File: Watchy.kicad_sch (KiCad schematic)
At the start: 67 parts, among them J1 FPC24(0.5MM), J2 Micro USB, J3 Battery, M1 Vibration_Motor, Q1 AO3400A, Q2 UMH3N, Q4 CJ2301, Q5 S8050, SW1 BTN, SW2 BTN, SW3 BTN, SW4 BTN, U1 ESP32-PICO-D4, U2 ME6211C33M5G-N, U3 CP2102, U4 BMA423, U5 TP4054, U6 PCF8563BS, Y1 32.768KHz

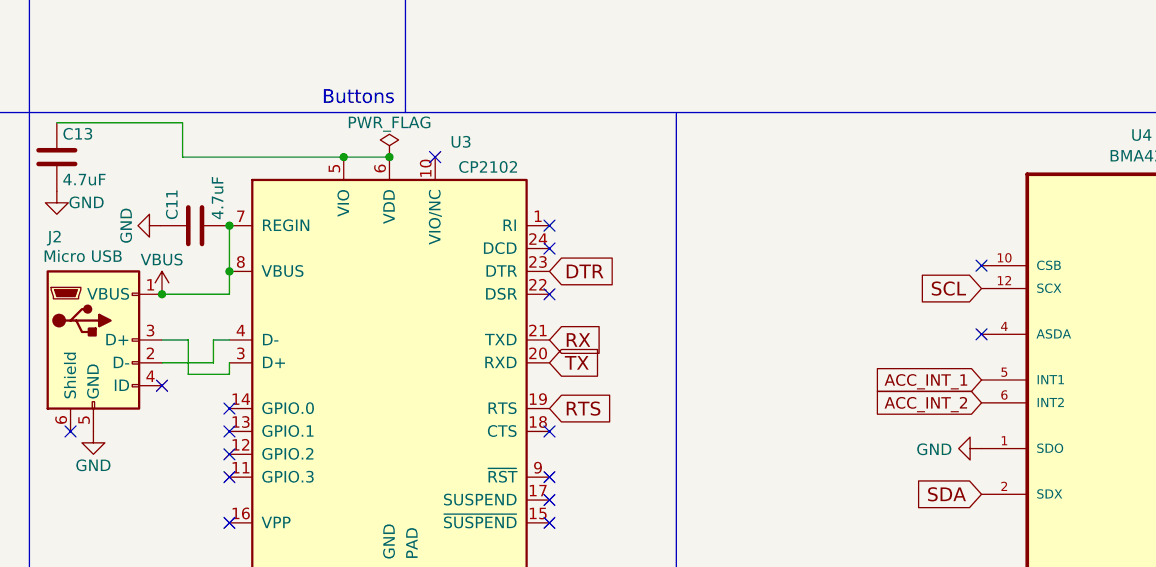
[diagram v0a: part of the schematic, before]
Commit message: cleanup of USB data lines
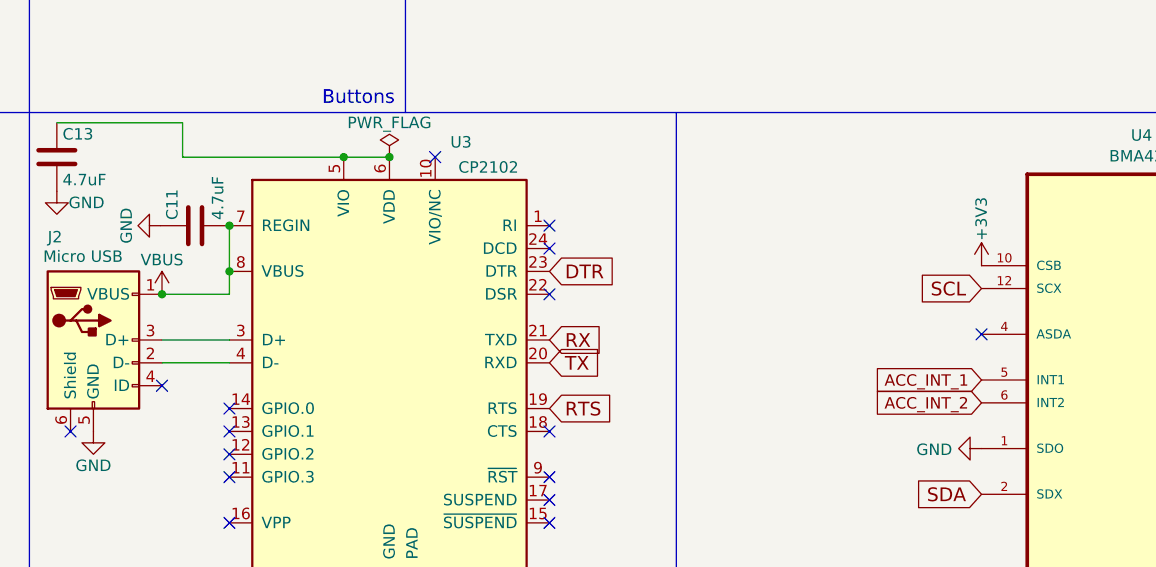
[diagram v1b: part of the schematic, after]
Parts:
- U3: footprint Housings_DFN_QFN:QFN-24-1EP_4x4mm_Pitch0.5mm -> Package_DFN_QFN:QFN-24-1EP_4x4mm_P0.5mm_EP2.6x2.6mm
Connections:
- net +3V3: now also U4.10 (CSB)
- no-connect marks 37 -> 36
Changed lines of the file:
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@@
   (no_connect (at 34.29 75.946))
   (no_connect (at 74.93 96.266))
-  (no_connect (at 210.947 127.889))
   (no_connect (at 34.29 70.866))
   (no_connect (at 162.941 146.304))
@@
     (stroke (width 0) (type default))
   )
-  (wire (pts (xy 119.888 136.144) (xy 122.809 136.144))
+  (wire (pts (xy 119.888 136.144) (xy 127.381 136.144))
     (stroke (width 0) (type default))
   )
@@
     (stroke (width 0) (type default))
   )
-  (wire (pts (xy 122.809 139.954) (xy 127.381 139.954))
-    (stroke (width 0) (type default))
-  )
-  (wire (pts (xy 125.603 136.144) (xy 127.381 136.144))
-    (stroke (width 0) (type default))
-  )
-  (wire (pts (xy 127.381 139.954) (xy 127.381 138.684))
-    (stroke (width 0) (type default))
-  )
-  (wire (pts (xy 122.809 136.144) (xy 122.809 139.954))
-    (stroke (width 0) (type default))
-  )
   (wire (pts (xy 19.304 185.42) (xy 19.304 187.96))
     (stroke (width 0) (type default))
@@
     (stroke (width 0) (type default))
   )
-  (wire (pts (xy 119.888 138.684) (xy 125.603 138.684))
+  (wire (pts (xy 119.888 138.684) (xy 127.381 138.684))
     (stroke (width 0) (type default))
   )
@@
     (stroke (width 0) (type default))
   )
-  (wire (pts (xy 125.603 138.684) (xy 125.603 136.144))
-    (stroke (width 0) (type default))
-  )
   (polyline (pts (xy 105.156 12.319) (xy 105.156 169.037))
     (stroke (width 0) (type default))
@@
       (effects (font (size 1.27 1.27)) (justify right))
     )
-    (property "Footprint" "Housings_DFN_QFN:QFN-24-1EP_4x4mm_Pitch0.5mm" (at 148.971 162.814 0)
+    (property "Footprint" "Package_DFN_QFN:QFN-24-1EP_4x4mm_P0.5mm_EP2.6x2.6mm" (at 148.971 162.814 0)
       (effects (font (size 1.27 1.27)) (justify left) hide)
     )
@@
         )
       )
+    )
+  )
+  (symbol (lib_id "power:+3V3") (at 210.947 127.889 0) (unit 1)
+    (in_bom yes) (on_board yes) (dnp no)
+    (property "Reference" "#PWR067" (at 210.947 131.699 0)
+      (effects (font (size 1.27 1.27)) hide)
+    )
+    (property "Value" "+3V3" (at 210.947 122.682 90)
+      (effects (font (size 1.27 1.27)))
+    )
+    (property "Footprint" "" (at 210.947 127.889 0)
+      (effects (font (size 1.27 1.27)) hide)
+    )
+    (property "Datasheet" "" (at 210.947 127.889 0)
+      (effects (font (size 1.27 1.27)) hide)
+    )
+    (pin "1")
+    (instances
+      (project "Watchy"
+        (path "/4168ccf9-7940-46a9-babd-bad8c703bb50"
+          (reference "#PWR067") (unit 1)
+        )
+      )

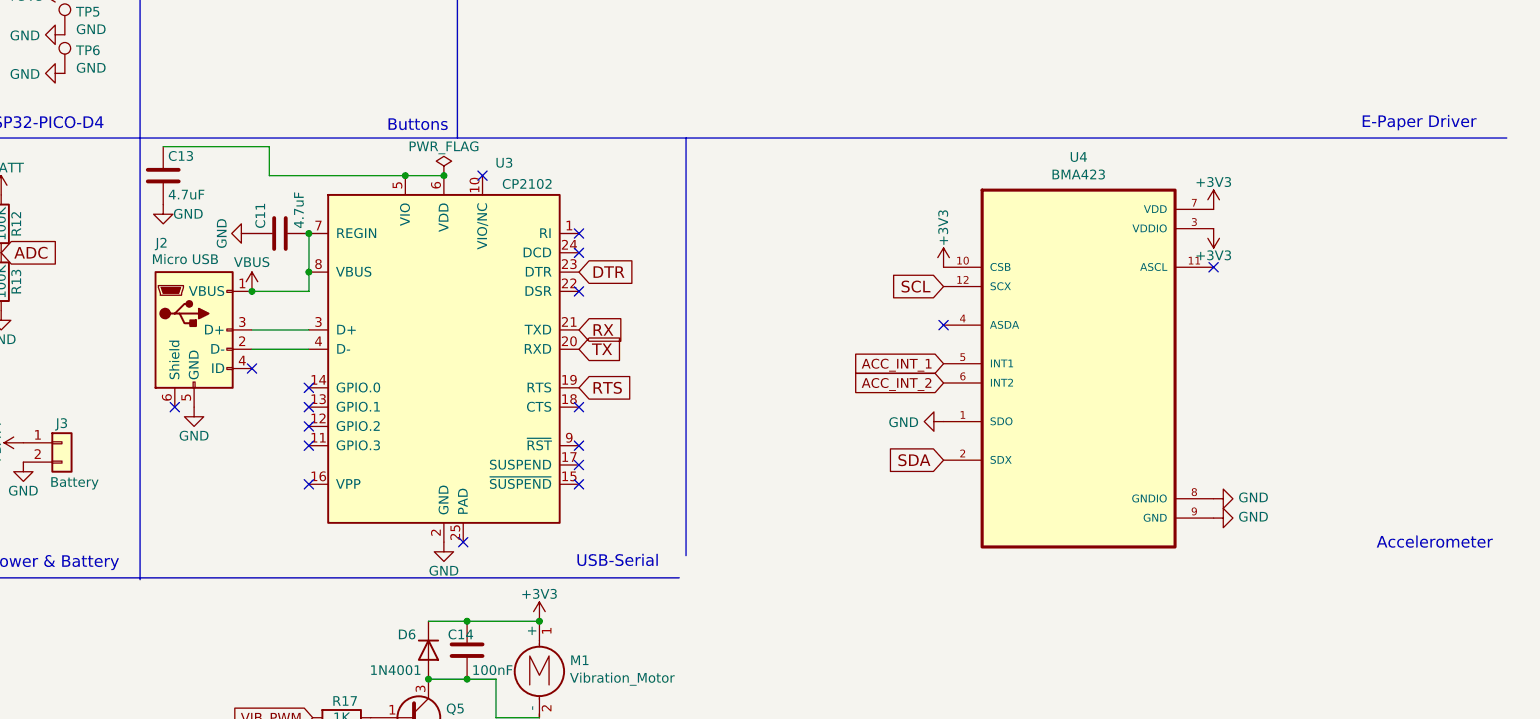
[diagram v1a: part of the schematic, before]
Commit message: replace micro usb with usb c in schematic
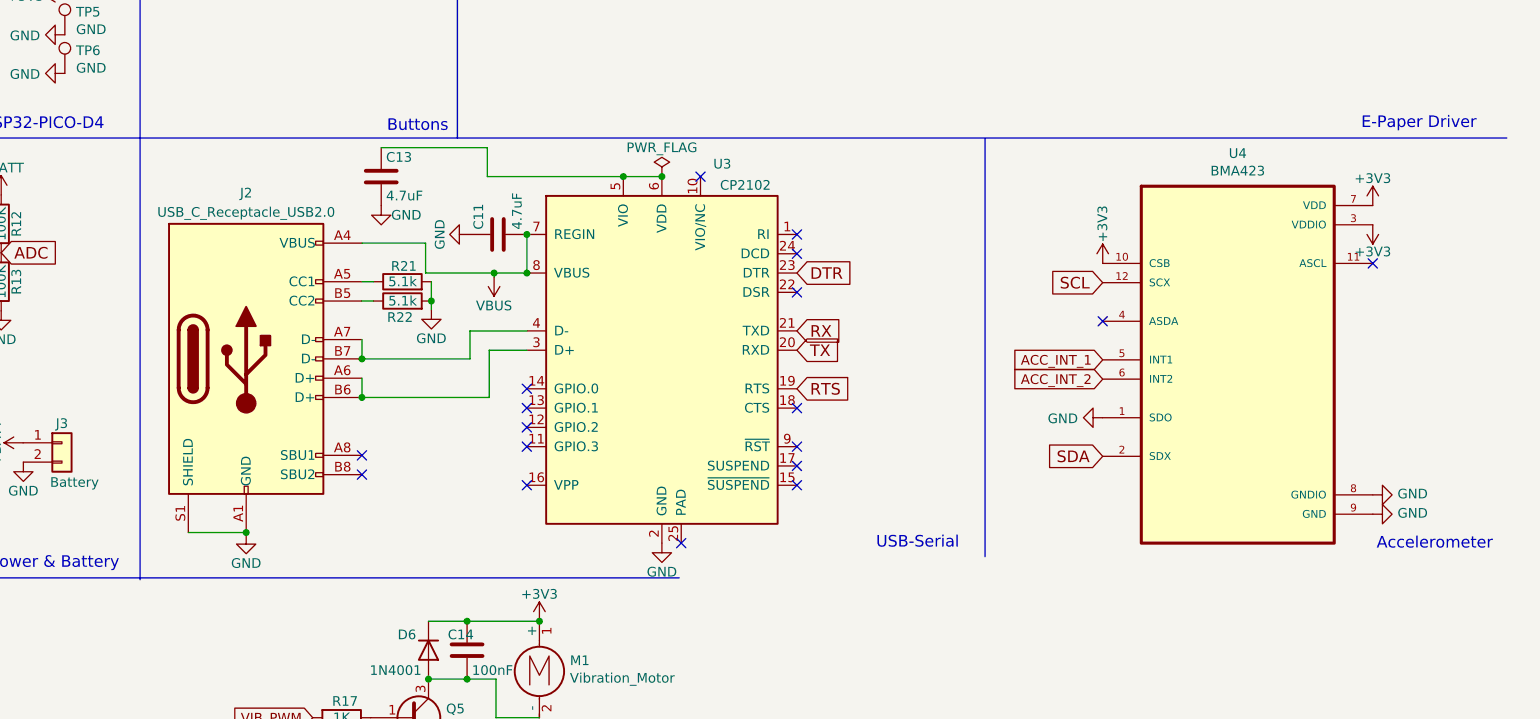
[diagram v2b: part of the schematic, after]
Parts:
- removed J2: Micro USB, Watchy:USB_Micro-B, symbol Connector:USB_OTG
- added J2: USB_C_Receptacle_USB2.0, Connector_USB:USB_C_Receptacle_Palconn_UTC16-G, symbol Connector:USB_C_Receptacle_USB2.0
- added R21, R22: 5.1k, Resistors_SMD:R_0402, symbol Device:R
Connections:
- net GND: now also J2.A1 (GND), J2.A12 (GND), J2.B1 (GND), J2.B12 (GND), J2.S1 (SHIELD), R21.2, R22.2
- net VBUS: now also J2.A4 (VBUS), J2.A9 (VBUS), J2.B4 (VBUS), J2.B9 (VBUS)
- net at U3.4 (D-): now also J2.A7 (D-), J2.B7 (D-)
- net at U3.3 (D+): now also J2.A6 (D+), J2.B6 (D+)
- new net: J2.B5 (CC2), R22.1
- new net: J2.A5 (CC1), R21.1
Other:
- moved on the sheet: C11, C13, U3, U4

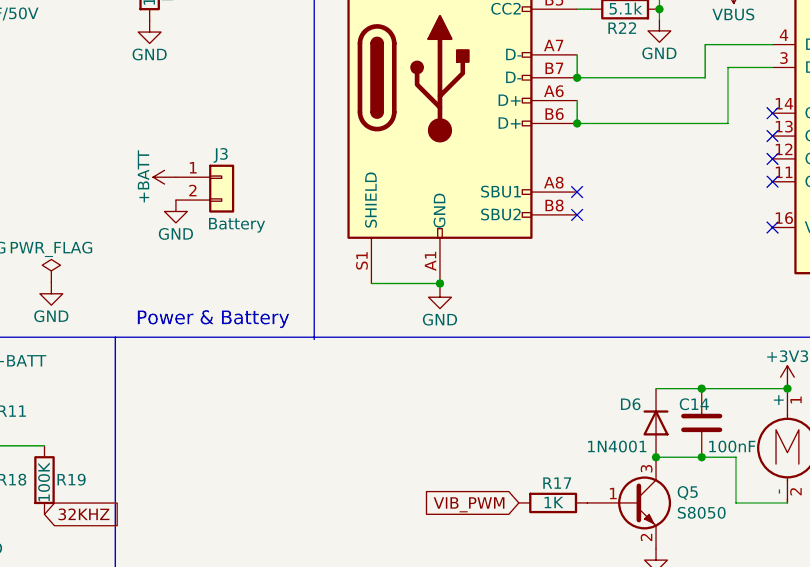
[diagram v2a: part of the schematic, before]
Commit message: remove usb c shield connection to ground
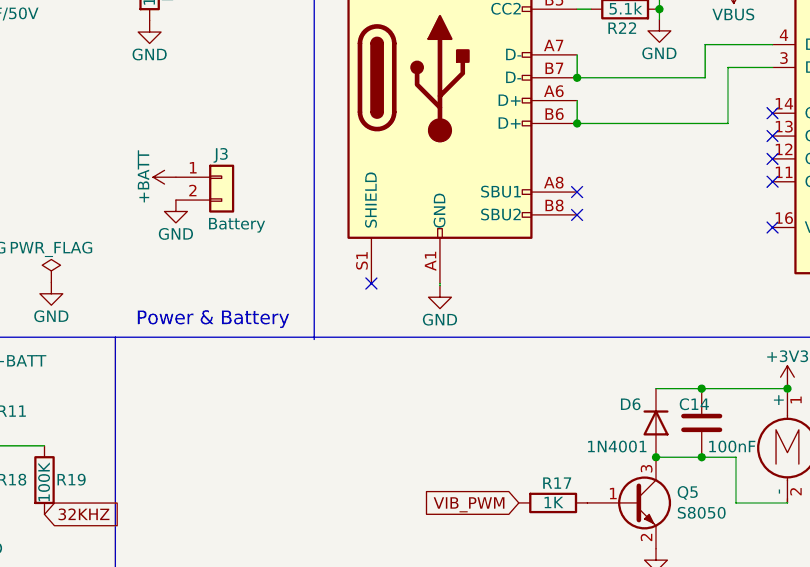
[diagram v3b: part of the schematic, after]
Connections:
- net GND: no longer J2.S1 (SHIELD)
- no-connect marks 36 -> 37
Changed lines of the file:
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@@
   (junction (at 28.829 126.619) (diameter 0) (color 0 0 0 0)
-  )
-  (junction (at 119.126 162.814) (diameter 0) (color 0 0 0 0)
   )
   (junction (at 168.783 115.951) (diameter 0) (color 0 0 0 0)
@@
   (junction (at 156.083 128.651) (diameter 0) (color 0 0 0 0)
   )
+  (no_connect (at 111.506 162.814))
   (no_connect (at 191.643 154.051))
   (no_connect (at 245.618 34.417))
@@
     (stroke (width 0) (type default))
   )
-  (wire (pts (xy 111.506 162.814) (xy 119.126 162.814))
-    (stroke (width 0) (type default))
-  )

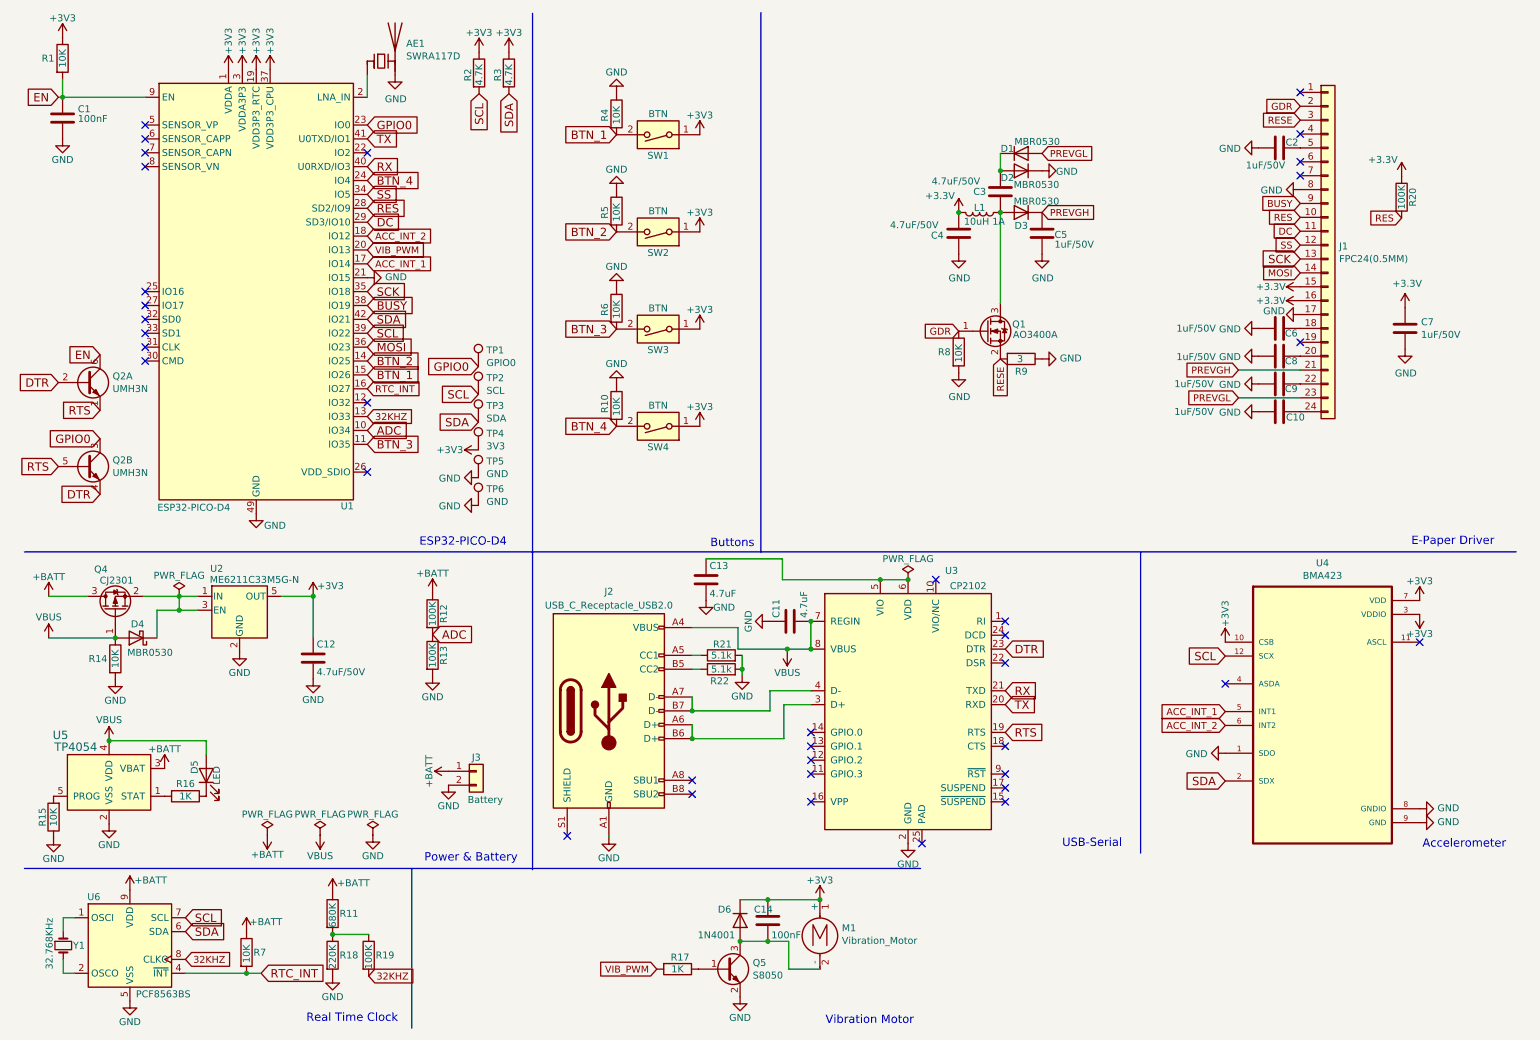
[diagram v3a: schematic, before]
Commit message: add charging status on gpio pin
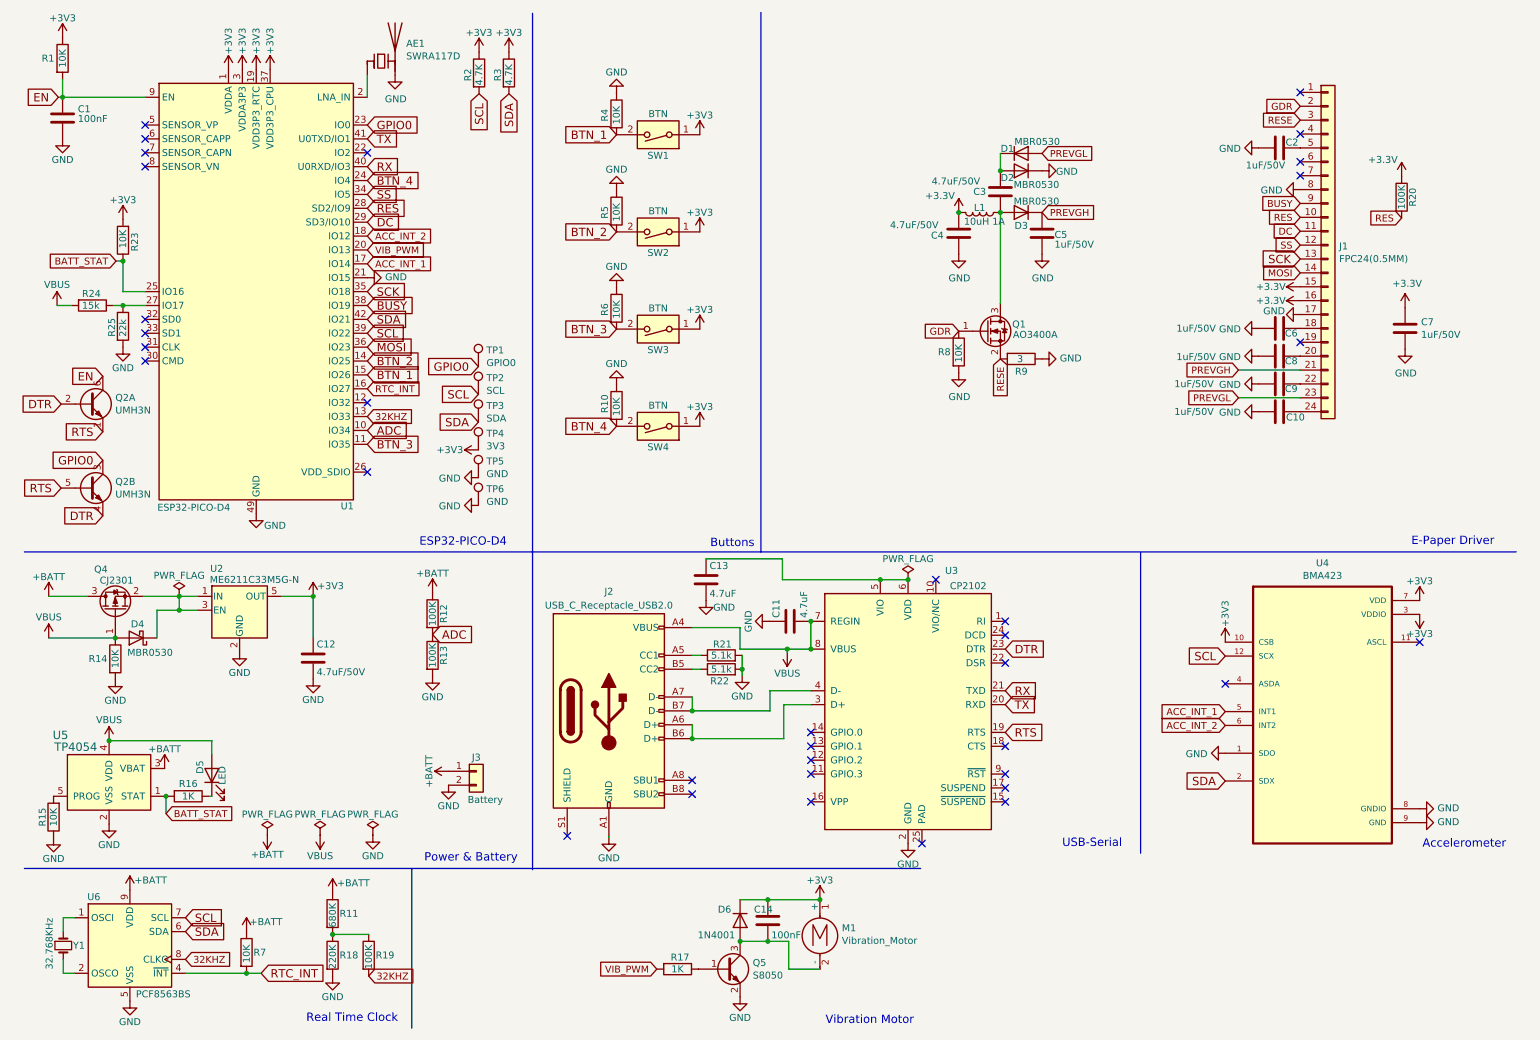
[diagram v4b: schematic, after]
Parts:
- added R23: 10K, Resistor_SMD:R_0402_1005Metric, symbol Device:R
- added R24: 15k, Resistor_SMD:R_0402_1005Metric, symbol Device:R
- added R25: 22k, Resistor_SMD:R_0402_1005Metric, symbol Device:R
- R21, R22: footprint Resistors_SMD:R_0402 -> Resistor_SMD:R_0402_1005Metric
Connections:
- net +3V3: now also R23.2
- net GND: now also R25.2
- net VBUS: now also R24.2
- net BATT_STAT: now reaches R16.2, U5.1 (STAT)
- net BATT_STAT: now also U1.25 (IO16), R23.1
- net at U1.27 (IO17): now also R24.1, R25.1
- no-connect marks 37 -> 35
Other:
- moved on the sheet: D5, Q2A, Q2B, R16
